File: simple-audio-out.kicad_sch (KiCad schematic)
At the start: 6 parts, among them J1 Conn_01x04, Q1 2N3904

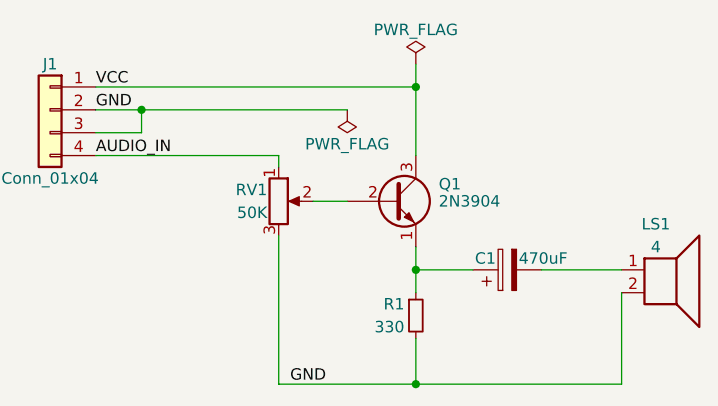
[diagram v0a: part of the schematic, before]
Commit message: revert to US symbols
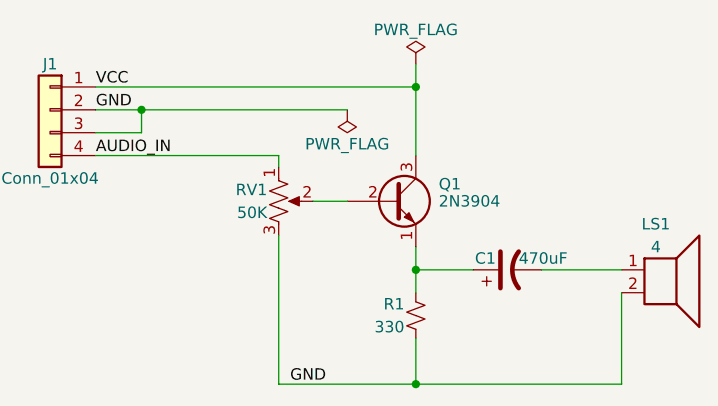
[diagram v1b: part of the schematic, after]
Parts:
- C1: symbol Device:C_Polarized -> Device:C_Polarized_US
- R1: symbol Device:R_Small -> Device:R_Small_US
- RV1: symbol Device:R_Potentiometer -> Device:R_Potentiometer_US
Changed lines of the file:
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@@
   (title_block
     (title "Simple audio out")
-    (date "2024-01-20")
+    (date "2024-01-21")
     (rev "0.0.1-DRAFT")
     (company "Sporniket")
@@
     )
   )
-  (symbol (lib_id "Device:R_Potentiometer") (at 88.9 55.88 0) (unit 1)
+  (symbol (lib_id "Device:R_Potentiometer_US") (at 88.9 55.88 0) (unit 1)
     (in_bom yes) (on_board yes) (dnp no)
     (property "Reference" "RV1" (at 87.63 54.61 0)
@@
     )
   )
-  (symbol (lib_id "Device:C_Polarized") (at 114.3 63.5 90) (unit 1)
+  (symbol (lib_id "Device:C_Polarized_US") (at 114.3 63.5 90) (unit 1)
     (in_bom yes) (on_board yes) (dnp no)
     (property "Reference" "C1" (at 113.03 62.23 90)
@@
       (effects (font (size 1.27 1.27)) (justify right))
     )
-    (property "Footprint" "" (at 118.11 62.5348 0)
+    (property "Footprint" "" (at 114.3 63.5 0)
       (effects (font (size 1.27 1.27)) hide)
     )
@@
     )
   )
-  (symbol (lib_id "Device:R_Small") (at 104.14 68.58 0) (unit 1)
+  (symbol (lib_id "Device:R_Small_US") (at 104.14 68.58 0) (unit 1)
     (in_bom yes) (on_board yes) (dnp no)
     (property "Reference" "R1" (at 102.87 67.31 0)

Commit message: footprint assigned
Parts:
- C1: footprint (none) -> Capacitor_THT:CP_Radial_D10.0mm_P3.80mm
- J1: footprint (none) -> Connector_PinHeader_2.54mm:PinHeader_1x04_P2.54mm_Horizontal
- LS1: footprint (none) -> Connector_PinHeader_2.54mm:PinHeader_1x02_P2.54mm_Horizontal
- R1: footprint (none) -> commons-passives_THT:Passive_THT_resistor_W2.54mm_L10.16mm
- RV1: footprint (none) -> Potentiometer_THT:Potentiometer_Runtron_RM-065_Vertical
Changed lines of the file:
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@@
       (effects (font (size 1.27 1.27)) (justify right))
     )
-    (property "Footprint" "" (at 88.9 55.88 0)
+    (property "Footprint" "Potentiometer_THT:Potentiometer_Runtron_RM-065_Vertical" (at 88.9 55.88 0)
       (effects (font (size 1.27 1.27)) hide)
     )
@@
       (effects (font (size 1.27 1.27)) (justify right))
     )
-    (property "Footprint" "" (at 114.3 63.5 0)
+    (property "Footprint" "Capacitor_THT:CP_Radial_D10.0mm_P3.80mm" (at 114.3 63.5 0)
       (effects (font (size 1.27 1.27)) hide)
     )
@@
       (effects (font (size 1.27 1.27)))
     )
-    (property "Footprint" "" (at 63.5 45.72 0)
+    (property "Footprint" "Connector_PinHeader_2.54mm:PinHeader_1x04_P2.54mm_Horizontal" (at 63.5 45.72 0)
       (effects (font (size 1.27 1.27)) hide)
     )
@@
       (effects (font (size 1.27 1.27)) (justify right))
     )
-    (property "Footprint" "" (at 104.14 68.58 0)
+    (property "Footprint" "commons-passives_THT:Passive_THT_resistor_W2.54mm_L10.16mm" (at 104.14 68.58 0)
       (effects (font (size 1.27 1.27)) hide)
     )
@@
       (effects (font (size 1.27 1.27)))
     )
-    (property "Footprint" "" (at 132.08 68.58 0)
+    (property "Footprint" "Connector_PinHeader_2.54mm:PinHeader_1x02_P2.54mm_Horizontal" (at 132.08 68.58 0)
       (effects (font (size 1.27 1.27)) hide)
     )

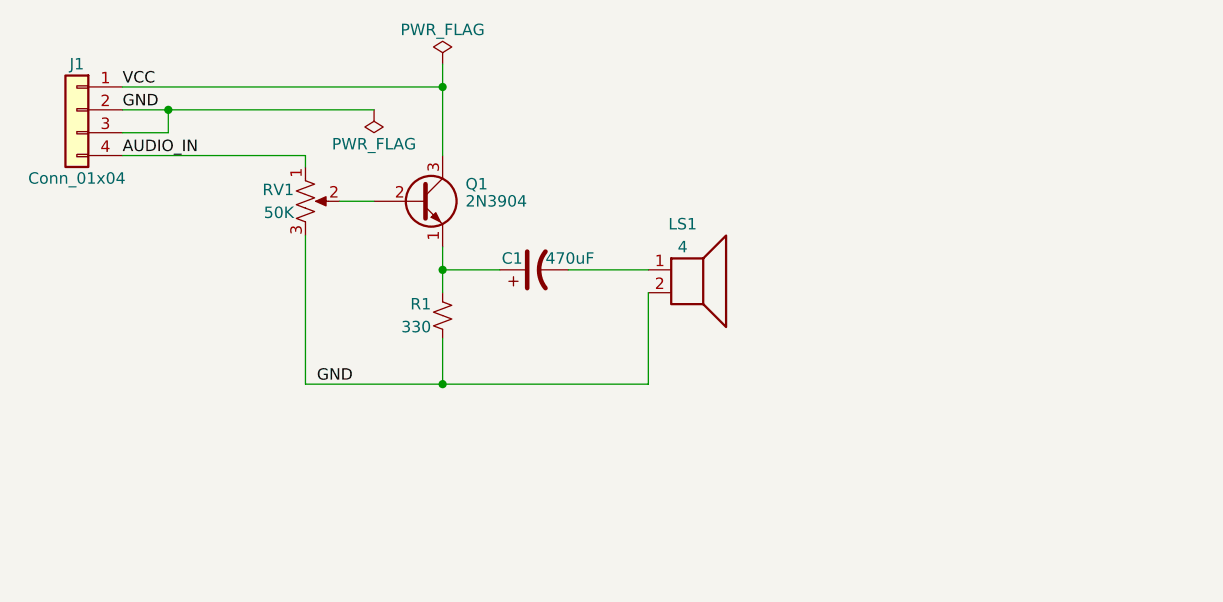
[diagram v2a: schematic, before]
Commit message: added mounting holes for speaker
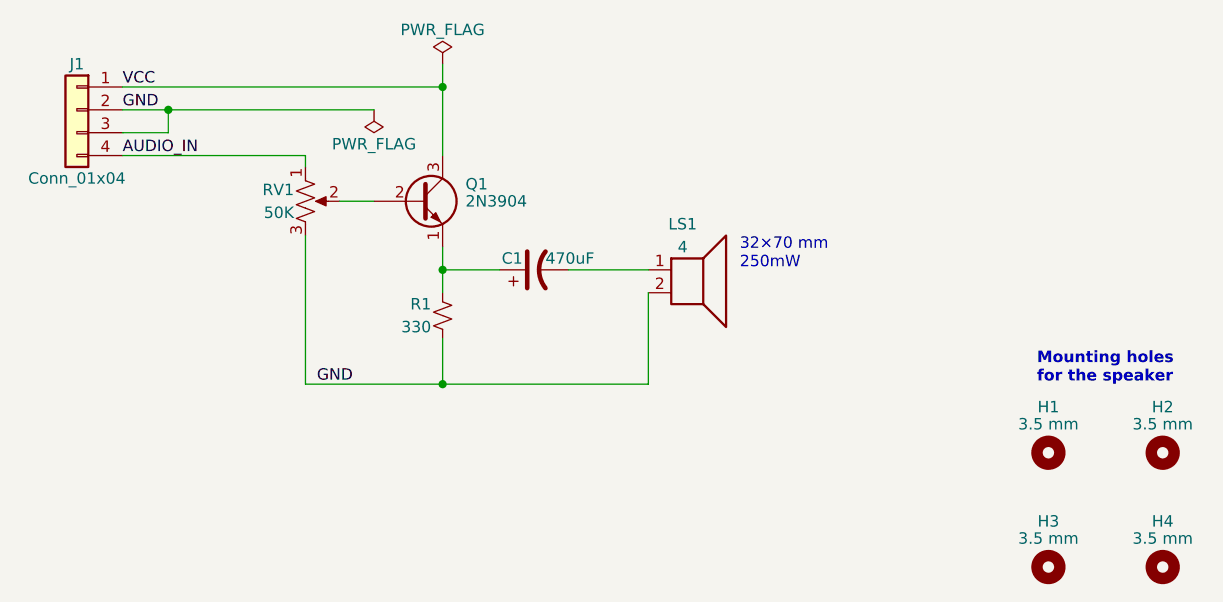
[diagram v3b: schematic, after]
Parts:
- added H1, H2, H3, H4: 3.5 mm, MountingHole:MountingHole_3.5mm, symbol Mechanical:MountingHole
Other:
- note added: "32×70 mm 250mW"
- note added: "Mounting holes for the speaker"
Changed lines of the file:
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@@
     (stroke (width 0) (type default))
   )
+  (text "Mounting holes\nfor the speaker" (at 170.18 76.2 0)
+    (effects (font (size 1.27 1.27) (thickness 0.254) bold) (justify left bottom))
+  )
+  (text "32×70 mm \n250mW " (at 137.16 63.5 0)
+    (effects (font (size 1.27 1.27)) (justify left bottom))
+  )
   (label "GND" (at 90.17 76.2 0) (fields_autoplaced)
     (effects (font (size 1.27 1.27)) (justify left bottom))
@@
         (path "/53c9bd77-cec4-4514-923d-07fb28dfd114"
           (reference "#FLG02") (unit 1)
+        )
+      )
+    )
+  )
+  (symbol (lib_id "Mechanical:MountingHole") (at 171.45 96.52 0) (unit 1)
+    (in_bom yes) (on_board yes) (dnp no)
+    (property "Reference" "H3" (at 171.45 91.44 0)
+      (effects (font (size 1.27 1.27)))
+    )
+    (property "Value" "3.5 mm" (at 171.45 93.345 0)
+      (effects (font (size 1.27 1.27)))
+    )
+    (property "Footprint" "MountingHole:MountingHole_3.5mm" (at 171.45 96.52 0)
+      (effects (font (size 1.27 1.27)) hide)
+    )
+    (property "Datasheet" "~" (at 171.45 96.52 0)
+      (effects (font (size 1.27 1.27)) hide)
+    )
+    (instances
+      (project "simple-audio-out"
+        (path "/53c9bd77-cec4-4514-923d-07fb28dfd114"
+          (reference "H3") (unit 1)
         )
       )
@@
     )
   )
+  (symbol (lib_id "Mechanical:MountingHole") (at 171.45 83.82 0) (unit 1)
+    (in_bom yes) (on_board yes) (dnp no)
+    (property "Reference" "H1" (at 171.45 78.74 0)
+      (effects (font (size 1.27 1.27)))
+    )
+    (property "Value" "3.5 mm" (at 171.45 80.645 0)
+      (effects (font (size 1.27 1.27)))
+    )
+    (property "Footprint" "MountingHole:MountingHole_3.5mm" (at 171.45 83.82 0)
+      (effects (font (size 1.27 1.27)) hide)
+    )
+    (property "Datasheet" "~" (at 171.45 83.82 0)
+      (effects (font (size 1.27 1.27)) hide)
+    )
+    (instances
+      (project "simple-audio-out"
+        (path "/53c9bd77-cec4-4514-923d-07fb28dfd114"
+          (reference "H1") (unit 1)
+        )
+      )
+    )
+  )
   (symbol (lib_id "Device:R_Small_US") (at 104.14 68.58 0) (unit 1)
     (in_bom yes) (on_board yes) (dnp no)
@@
         )
       )
+    )
+  )
+  (symbol (lib_id "Mechanical:MountingHole") (at 184.15 83.82 0) (unit 1)
+    (in_bom yes) (on_board yes) (dnp no)
+    (property "Reference" "H2" (at 184.15 78.74 0)
+      (effects (font (size 1.27 1.27)))
+    )
+    (property "Value" "3.5 mm" (at 184.15 80.645 0)
+      (effects (font (size 1.27 1.27)))
+    )
+    (property "Footprint" "MountingHole:MountingHole_3.5mm" (at 184.15 83.82 0)
+      (effects (font (size 1.27 1.27)) hide)
+    )
+    (property "Datasheet" "~" (at 184.15 83.82 0)
+      (effects (font (size 1.27 1.27)) hide)
+    )
+    (instances
+      (project "simple-audio-out"
+        (path "/53c9bd77-cec4-4514-923d-07fb28dfd114"
+          (reference "H2") (unit 1)
+        )
+      )
+    )
+  )
+  (symbol (lib_id "Mechanical:MountingHole") (at 184.15 96.52 0) (unit 1)
+    (in_bom yes) (on_board yes) (dnp no)
+    (property "Reference" "H4" (at 184.15 91.44 0)
+      (effects (font (size 1.27 1.27)))
+    )
+    (property "Value" "3.5 mm" (at 184.15 93.345 0)
+      (effects (font (size 1.27 1.27)))
+    )
+    (property "Footprint" "MountingHole:MountingHole_3.5mm" (at 184.15 96.52 0)
+      (effects (font (size 1.27 1.27)) hide)
+    )
+    (property "Datasheet" "~" (at 184.15 96.52 0)
+      (effects (font (size 1.27 1.27)) hide)
+    )
+    (instances
+      (project "simple-audio-out"
+        (path "/53c9bd77-cec4-4514-923d-07fb28dfd114"
+          (reference "H4") (unit 1)
+        )
+      )
